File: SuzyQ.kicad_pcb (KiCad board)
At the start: 2 copper layers, 8.6 x 7.5 mm, 3 parts, among them P1 USB_C_Plug

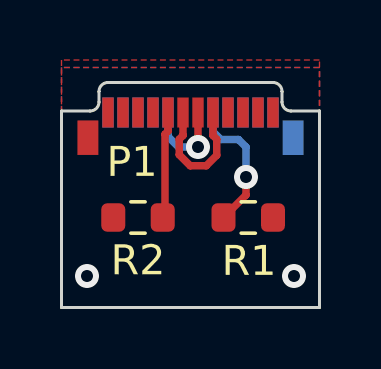
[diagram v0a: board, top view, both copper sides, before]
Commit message: Radius'd PCB corners, added fiducial
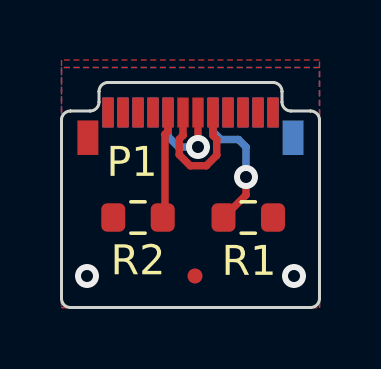
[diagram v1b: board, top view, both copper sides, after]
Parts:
- added REF**: Fiducial_0.5mm_Mask1mm, Fiducial:Fiducial_0.5mm_Mask1mm, F.Cu at (136.4, 77.5)
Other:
- outline, holes or cut-outs redrawn
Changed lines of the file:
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@@
+		)
+	)
+	(footprint "Fiducial:Fiducial_0.5mm_Mask1mm"
+		(layer "F.Cu")
+		(at 136.4 77.45)
+		(descr "Circular Fiducial, 0.5mm bare copper, 1mm soldermask opening (Level C)")
+		(tags "fiducial")
+		(property "Reference" "REF**"
+			(at 0 -1.5 0)
+			(layer "F.SilkS")
+			(hide yes)
+			(effects
+				(font
+					(size 1 1)
+					(thickness 0.15)
+				)
+			)
+		)
+		(property "Value" "Fiducial_0.5mm_Mask1mm"
+			(at 0 1.5 0)
+			(layer "F.Fab")
+			(effects
+				(font
+					(size 1 1)
+					(thickness 0.15)
+				)
+			)
+		)
+		(property "Footprint" "Fiducial:Fiducial_0.5mm_Mask1mm"
+			(at 0 0 0)
+			(unlocked yes)
+			(layer "F.Fab")
+			(hide yes)
+			(effects
+				(font
+					(size 1.27 1.27)
+				)
+			)
+		)
+		(property "Datasheet" ""
+			(at 0 0 0)
+			(unlocked yes)
+			(layer "F.Fab")
+			(hide yes)
+			(effects
+				(font
+					(size 1.27 1.27)
+				)
+			)
+		)
+		(property "Description" ""
+			(at 0 0 0)
+			(unlocked yes)
+			(layer "F.Fab")
+			(hide yes)
+			(effects
+				(font
+					(size 1.27 1.27)
+				)
+			)
+		)
+		(attr smd board_only exclude_from_bom dnp)
+		(fp_circle
+			(center 0 0)
+			(end 0.75 0)
+			(stroke
+				(width 0.05)
+				(type solid)
+			)
+			(fill none)
+			(layer "F.CrtYd")
+		)
+		(fp_circle
+			(center 0 0)
+			(end 0.5 0)
+			(stroke
+				(width 0.1)
+				(type solid)
+			)
+			(fill none)
+			(layer "F.Fab")
+		)
+		(fp_text user "${REFERENCE}"
+			(at 0 0 0)
+			(layer "F.Fab")
+			(effects
+				(font
+					(size 0.2 0.2)
+					(thickness 0.04)
+				)
+			)
+		)
+		(pad "" smd circle
+			(at 0 0)
+			(size 0.5 0.5)
+			(layers "F.Cu" "F.Mask")
+			(solder_mask_margin 0.25)
+			(clearance 0.25)
 		)
 	)
@@
 		(layer "Edge.Cuts")
 	)
-	(gr_line
-		(start 131.95 71.95)
-		(end 131.95 78.5)
+	(gr_arc
+		(start 140.55 78.2)
+		(mid 140.462132 78.412132)
+		(end 140.25 78.5)
+		(stroke
+			(width 0.1)
+			(type default)
+		)
+		(layer "Edge.Cuts")
+	)
+	(gr_line
+		(start 131.95 72.25)
+		(end 131.95 78.2)
 		(stroke
 			(width 0.1)
@@
 		(layer "Edge.Cuts")
 	)
-	(gr_line
-		(start 140.55 71.95)
-		(end 140.55 78.5)
+	(gr_arc
+		(start 131.95 72.25)
+		(mid 132.037868 72.037868)
+		(end 132.25 71.95)
+		(stroke
+			(width 0.1)
+			(type default)
+		)
+		(layer "Edge.Cuts")
+	)
+	(gr_arc
+		(start 132.25 78.5)
+		(mid 132.037868 78.412132)
+		(end 131.95 78.2)
+		(stroke
+			(width 0.1)
+			(type default)
+		)
+		(layer "Edge.Cuts")
+	)
+	(gr_line
+		(start 140.55 72.25)
+		(end 140.55 78.2)
 		(stroke
 			(width 0.1)
@@
 	)
 	(gr_line
-		(start 131.95 78.5)
-		(end 140.55 78.5)
+		(start 132.25 78.5)
+		(end 140.25 78.5)
 		(stroke
 			(width 0.1)
@@
 		(layer "Edge.Cuts")
 	)
+	(gr_arc
+		(start 140.25 71.95)
+		(mid 140.462132 72.037868)
+		(end 140.55 72.25)
+		(stroke
+			(width 0.1)
+			(type default)
+		)
+		(layer "Edge.Cuts")
+	)
 	(gr_line
 		(start 139.3 71.3)
@@
 	)
 	(gr_line
-		(start 131.95 71.95)
+		(start 132.25 71.95)
 		(end 132.9 71.95)
 		(stroke
@@
 	(gr_line
 		(start 139.6 71.95)
-		(end 140.55 71.95)
-		(stroke
-			(width 0.1)
+		(end 140.25 71.95)
+		(stroke
+			(width 0.1)
